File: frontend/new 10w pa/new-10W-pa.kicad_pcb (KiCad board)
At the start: 2 copper layers, 100 x 100 mm, 177 parts, among them K1 D3002, K2 D3002, K3 D3002, K4 D3002, K5 D3002, K6 D3002, P1 CONN_01X02, P2 CONN_02X01, P3 From HL CN3, P4 CONN_01X02, P5 CONN_01X02, P6 CONN_01X01, P7 From FE CN2, P8 CONN_01X08, P9 CONN_02X05, Q1 2N3906, Q3 RD16HHF1, T1 TRANSFO, T2 OUT_TRANSF, U1 74HC14, U2 74HC14, U3 TPIC6B595, U4 TPIC6B595, U5 TPIC6B595, U6 TPIC6B595, U7 LP2951-50D

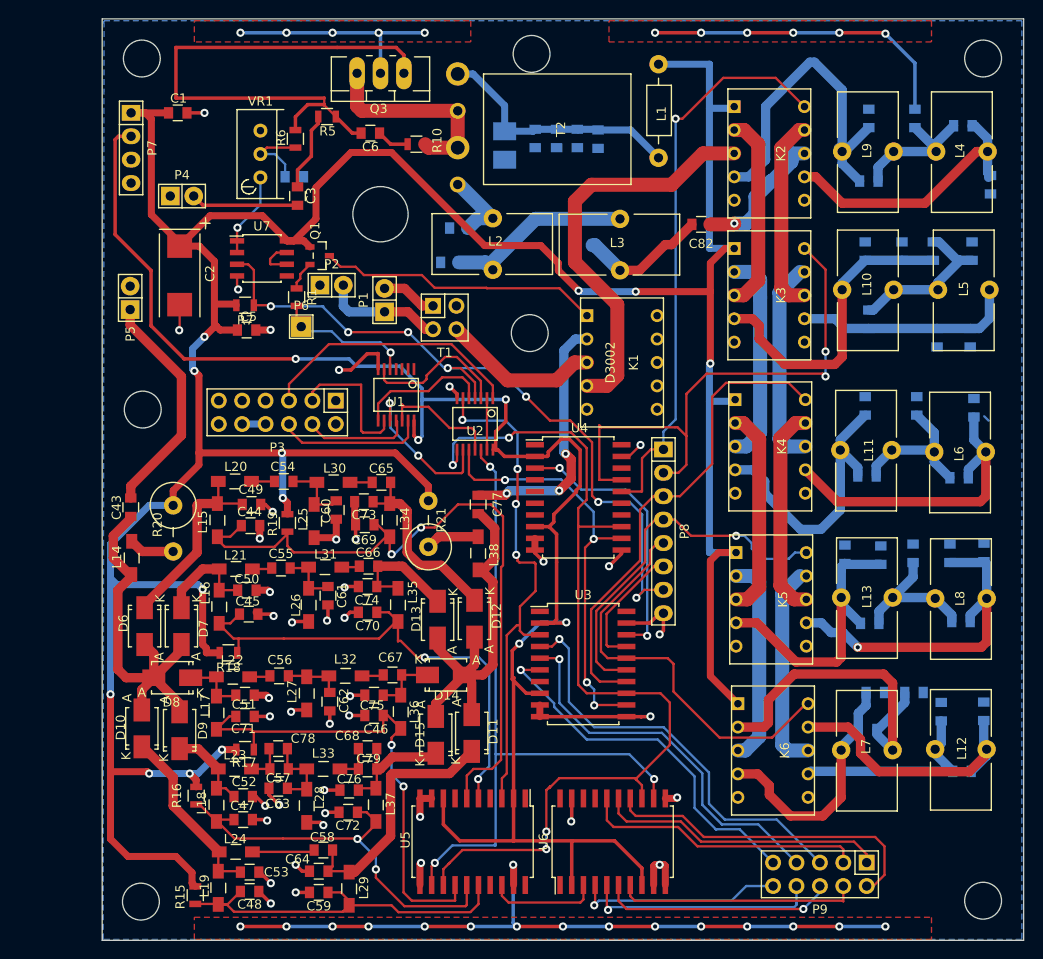
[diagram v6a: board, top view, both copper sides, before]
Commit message: Changes for new J16 approach
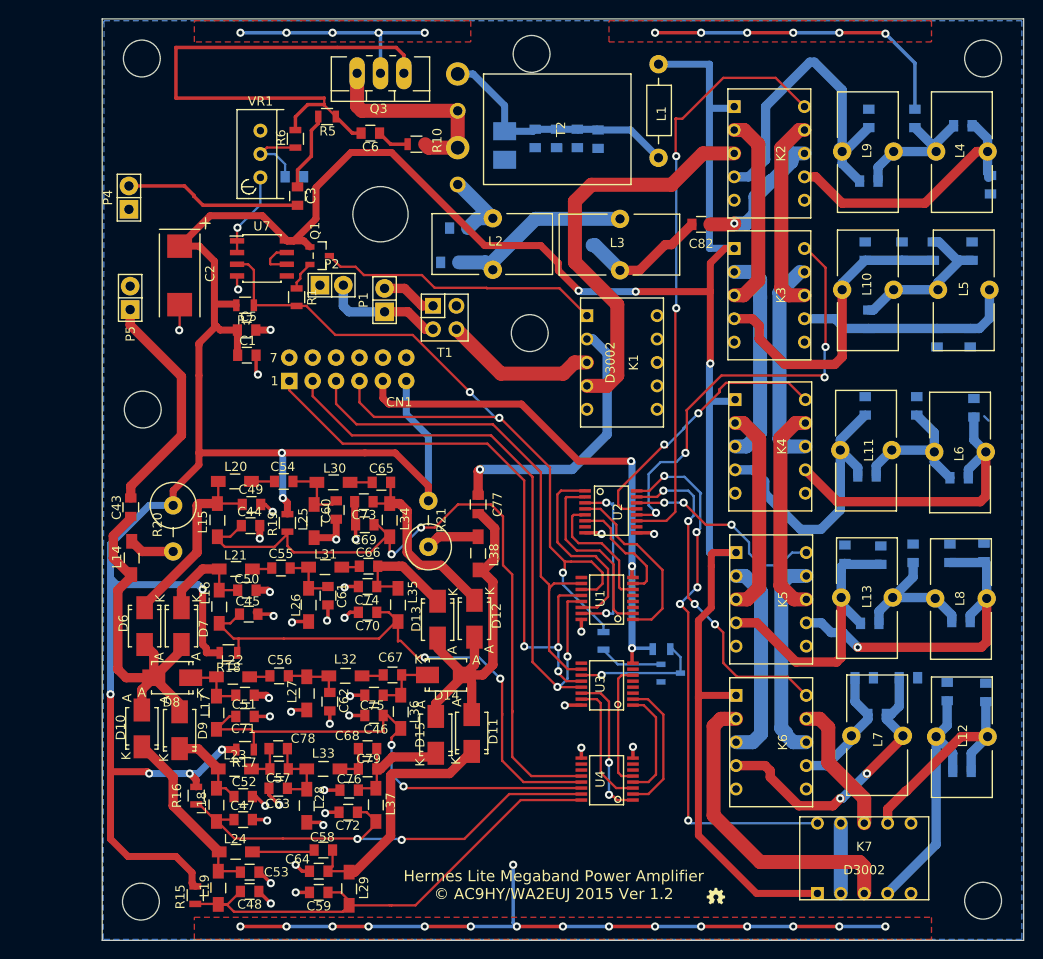
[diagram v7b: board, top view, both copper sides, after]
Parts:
- removed P3: From HL CN3, Pin_Headers:Pin_Header_Straight_2x06
- removed P6: CONN_01X01, Pin_Headers:Pin_Header_Straight_1x01
- removed P7: From FE CN2, Pin_Headers:Pin_Header_Straight_1x04
- removed P8: CONN_01X08, Pin_Headers:Pin_Header_Straight_1x08
- removed P9: CONN_02X05, Pin_Headers:Pin_Header_Straight_2x05
- removed U5, U6: TPIC6B595, Housings_SOIC:SOIC-20_7.5x12.8mm_Pitch1.27mm
- added CN1: BREAKOUT, HERMESLITE:BREAKOUT, F.Cu at (120.3, 89.3)
- added G***: OSHW-logo_silkscreen-front_2mm, HERMESLITE:OSHW-logo_silkscreen-front_2mm, F.Cu at (166.6, 145.2)
- added K7: D3002, HERMESLITE:D3002, F.Cu at (182.7, 141.1)
- added Q2: 2N3904, Transistors_SMD:sot23, B.Cu at (161.7, 121.0)
- added R2: 4.99k, HERMESLITE:R_0805, B.Cu at (154.4, 117.5)
- added R3: 4.99k, HERMESLITE:R_0805, B.Cu at (160.7, 118.4)
- U1: value 74HC14 -> 4028; footprint SMD_Packages:TSSOP-14 -> SMD_Packages:TSSOP-16
- U2: value 74HC14 -> ULN2003LV; footprint SMD_Packages:TSSOP-14 -> SMD_Packages:TSSOP-16
- U3: value TPIC6B595 -> 4028; footprint Housings_SOIC:SOIC-20_7.5x12.8mm_Pitch1.27mm -> SMD_Packages:TSSOP-16
- U4: value TPIC6B595 -> ULN2003LV; footprint Housings_SOIC:SOIC-20_7.5x12.8mm_Pitch1.27mm -> SMD_Packages:TSSOP-16
- moved U1 31.8 mm to (154.8, 112.9), turned to 90 degrees
- moved U4 30.7 mm to (154.8, 132.5), turned to 90 degrees
- moved C1 27.3 mm to (115.7, 86.5)
- moved U2 17.6 mm to (155.2, 103.5), turned to 270 degrees
- moved L7 15.8 mm to (180.8, 121.2), turned to 270 degrees
- moved P4 5.76 mm to (102.9, 69.4), turned to 90 degrees
- moved C20 5.63 mm to (182.7, 121.5)
- moved C26 3.94 mm to (187.5, 121.5)
- moved U3 3.40 mm to (154.8, 122.2), turned to 90 degrees
- moved C37 2.28 mm to (191.7, 123.0)
- moved C30 2.06 mm to (195.9, 123.1)
- moved C24 1.93 mm to (184.1, 125.5), turned to 180 degrees
- moved L12 1.37 mm to (196.6, 134.5)
- moved K6 0.92 mm to (172.6, 128.5)
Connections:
- K6 pad 2: Net-(C20-Pad1) -> Net-(K6-Pad2)
- K6 pad 7: Net-(C35-Pad1) -> Net-(C20-Pad1)
- K6 pad 9: Net-(C30-Pad1) -> Net-(K6-Pad9)
- R1 pad 2: Net-(P6-Pad1) -> #PTT
- R7 pad 1: /PTT -> #PTT
- U1 pad 10: Net-(U1-Pad10) -> A
- U1 pad 11: Net-(P3-Pad4) -> #PTT
- U1 pad 12: Net-(U1-Pad12) -> C
- U1 pad 13: Net-(P3-Pad6) -> B
- U1 pad 14: +5V -> Net-(U1-Pad14)
- U1 pad 5: Net-(P6-Pad1) -> Net-(U1-Pad5)
- U1 pad 7: GND -> Net-(U1-Pad7)
- U1 pad 8: Net-(U1-Pad8) -> 5V
- U2 pad 1: Net-(P3-Pad5) -> Net-(U1-Pad14)
- U2 pad 10: TX-Load -> Net-(U2-Pad10)
- U2 pad 11: Net-(U1-Pad12) -> Net-(K2-Pad10)
- U2 pad 12: RX-Load -> Net-(K3-Pad10)
- U2 pad 13: Net-(U2-Pad13) -> Net-(K4-Pad10)
- U2 pad 14: +5V -> Net-(K5-Pad10)
- U2 pad 2: Net-(U2-Pad13) -> Net-(U1-Pad2)
- U2 pad 3: Net-(U1-Pad6) -> Net-(U1-Pad15)
- U2 pad 4: /PTT -> Net-(U1-Pad1)
- U2 pad 5: Net-(U1-Pad8) -> Net-(U1-Pad6)
- U2 pad 6: SPI-DATA -> Net-(U1-Pad7)
- U2 pad 7: GND -> Net-(U2-Pad7)
- U2 pad 8: SPI-CLK -> GND
- U2 pad 9: Net-(U1-Pad10) -> GND
- U3 pad 1: (no net) -> Net-(U3-Pad1)
- U3 pad 10: GND -> A
- U3 pad 11: GND -> PTT
- U3 pad 12: TX-Load -> C
- U3 pad 13: SPI-CLK -> B
- U3 pad 14: Net-(K4-Pad10) -> Net-(U3-Pad14)
- U3 pad 15: Net-(K5-Pad10) -> Net-(U3-Pad15)
- U3 pad 16: Net-(K6-Pad10) -> GND
- U3 pad 2: +5V -> Net-(U3-Pad2)
- U3 pad 3: SPI-DATA -> Net-(U3-Pad3)
- U3 pad 4: ANT1 -> Net-(U3-Pad4)
- U3 pad 5: ANT2 -> Net-(U3-Pad5)
- U3 pad 6: ANT3 -> Net-(U3-Pad6)
- U3 pad 8: +5V -> 5V
- U3 pad 9: GND -> Net-(U3-Pad9)
- U4 pad 1: (no net) -> Net-(U3-Pad14)
- U4 pad 10: GND -> Net-(U4-Pad10)
- U4 pad 11: GND -> Net-(U4-Pad11)
- U4 pad 12: TX-Load -> Net-(C44-Pad1)
- U4 pad 13: SPI-CLK -> Net-(C45-Pad1)
- U4 pad 14: Net-(U4-Pad14) -> Net-(C46-Pad1)
- U4 pad 15: Net-(U4-Pad15) -> Net-(C47-Pad1)
- U4 pad 16: Net-(K2-Pad10) -> Net-(C48-Pad1)
- U4 pad 2: +5V -> Net-(U3-Pad2)
- U4 pad 3: Net-(U3-Pad18) -> Net-(U3-Pad15)
- U4 pad 4: Net-(U4-Pad4) -> Net-(U3-Pad1)
- U4 pad 5: Net-(U4-Pad5) -> Net-(U3-Pad6)
- U4 pad 8: +5V -> GND
- U7 pad 3: /PTT -> #PTT
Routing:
- net +5V: track 183.6 -> 0.00 mm, vias 5 -> 0
- net GND: track 251.3 -> 127.4 mm, vias 69 -> 47
- net SPI-CLK: track 105.4 -> 0.00 mm, vias 4 -> 0
- net #PTT: track 0.00 -> 92.5 mm, vias 0 -> 3
- net /PTT: track 79.0 -> 0.00 mm, vias 7 -> 0
- net (no net): track 0.67 -> 77.7 mm, vias 0 -> 16
- net RX-Load: track 74.1 -> 0.00 mm, vias 3 -> 0
- net B: track 0.00 -> 67.0 mm, vias 0 -> 2
- net C: track 0.00 -> 66.1 mm, vias 0 -> 3
- net Net-(K7-Pad10): track 0.00 -> 59.6 mm, vias 0 -> 5
- net 5V: track 0.00 -> 57.2 mm, vias 0 -> 3
- net A: track 0.00 -> 55.8 mm
- net SPI-DATA: track 55.7 -> 0.00 mm, vias 4 -> 0
- net TX-Load: track 46.4 -> 0.00 mm, vias 4 -> 0
- net ANT1: track 46.1 -> 0.00 mm, vias 1 -> 0
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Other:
- board text added: "Hermes Lite Megaband Power Amplifier © AC9HY/WA2EUJ 2015 Ver 1.2"
- board text removed: "AC9HY/WA2EUJ PA Ver 1.0"

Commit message: Final pcd changes
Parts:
- removed G***: OSHW-logo_silkscreen-front_2mm, HERMESLITE:OSHW-logo_silkscreen-front_2mm
- removed Q2: 2N3904, Transistors_SMD:sot23
- removed R1: 1k, HERMESLITE:R_0805
- removed R2, R3: 4.99k, HERMESLITE:R_0805
- removed R7: 10k, HERMESLITE:R_0805
- removed U4: ULN2003LV, SMD_Packages:TSSOP-16
- added C83: 1000pF, HERMESLITE:C_0805, F.Cu at (127.2, 94.6)
- added C84: 0.01uF, HERMESLITE:C_0805, F.Cu at (124.1, 95.5)
- added C85: 0.01uF, HERMESLITE:C_0805, F.Cu at (130.3, 95.8)
- added D1: DIODE, Diodes_SMD:Diode-SMA_Standard, F.Cu at (137.6, 142.0)
- added D16: DIODE, Diodes_SMD:Diode-SMA_Standard, F.Cu at (106.8, 114.4)
- added D17: DIODE, Diodes_SMD:Diode-SMA_Standard, F.Cu at (149.0, 113.7)
- added D2: DIODE, Diodes_SMD:Diode-SMA_Standard, F.Cu at (140.7, 137.2)
- added D3: DIODE, Diodes_SMD:Diode-SMA_Standard, F.Cu at (144.0, 135.2)
- added D4: DIODE, Diodes_SMD:Diode-SMA_Standard, F.Cu at (149.4, 126.0)
- added D5: DIODE, Diodes_SMD:Diode-SMA_Standard, F.Cu at (145.3, 94.4)
- added L39: 4700nH, HERMESLITE:Choke_SMD_1206_Standard, F.Cu at (119.9, 94.5)
- added L40: 4700uH, HERMESLITE:Choke_SMD_1206_Standard, F.Cu at (134.6, 94.6)
- added Q4: 2N7000, SMD_Packages:SOT-23-GDS, F.Cu at (140.1, 93.4)
- added R13: 1k, HERMESLITE:R_0805, F.Cu at (135.6, 91.6)
- added R14: 1k, HERMESLITE:R_0805, F.Cu at (119.9, 96.3)
- Q1: value 2N3906 -> 2N7000; footprint Transistors_SMD:sot23 -> SMD_Packages:SOT-23-GDS
- U1: value 4028 -> 4050; footprint SMD_Packages:TSSOP-16 -> Housings_SOIC:SOIC-16_3.9x9.9mm_Pitch1.27mm
- U2: value ULN2003LV -> 74LS145; footprint SMD_Packages:TSSOP-16 -> Housings_SOIC:SOIC-16_3.9x9.9mm_Pitch1.27mm
- U3: value 4028 -> 74LS145; footprint SMD_Packages:TSSOP-16 -> Housings_SOIC:SOIC-16_3.9x9.9mm_Pitch1.27mm
- moved CN1 65.0 mm to (161.3, 139.8), turned to 180 degrees
- moved U1 17.7 mm to (158.4, 130.2), turned to 0 degrees
- moved U3 9.94 mm to (158.3, 112.9), turned to 180 degrees
- moved R21 8.96 mm to (142.9, 99.9)
- moved L38 6.74 mm to (146.5, 104.4)
- moved C77 6.60 mm to (146.4, 99.2)
- moved C44 5.48 mm to (121.4, 103.6)
- moved C59 5.48 mm to (128.8, 143.4)
- moved C63 5.48 mm to (124.4, 132.1)
- moved C64 5.48 mm to (128.8, 141.1)
- moved C67 5.48 mm to (136.8, 119.8)
- moved C69 5.48 mm to (133.8, 103.5)
- moved C75 5.48 mm to (134.8, 122.0)
- moved D11 5.48 mm to (145.4, 126.1)
- moved D15 5.48 mm to (141.5, 126.3)
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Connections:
- CN1 pad 1: C -> Net-(CN1-Pad1)
- CN1 pad 2: B -> Net-(CN1-Pad2)
- CN1 pad 3: A -> Net-(CN1-Pad3)
- CN1 pad 4: #PTT -> Net-(CN1-Pad4)
- K1 pad 1: Net-(K1-Pad1) -> +12V
- K1 pad 10: GND -> Net-(K1-Pad10)
- U1 pad 1: Net-(U1-Pad1) -> 5V
- U1 pad 11: #PTT -> Net-(CN1-Pad4)
- U1 pad 12: C -> Net-(U1-Pad12)
- U1 pad 13: B -> (no net)
- U1 pad 14: Net-(U1-Pad14) -> (no net)
- U1 pad 15: Net-(U1-Pad15) -> (no net)
- U1 pad 16: GND -> (no net)
- U1 pad 2: Net-(U1-Pad2) -> D
- U1 pad 3: Net-(U1-Pad3) -> Net-(CN1-Pad7)
- U1 pad 4: Net-(U1-Pad4) -> C
- U1 pad 5: Net-(U1-Pad5) -> Net-(CN1-Pad1)
- U1 pad 6: Net-(U1-Pad6) -> B
- U1 pad 7: Net-(U1-Pad7) -> Net-(CN1-Pad2)
- U1 pad 8: 5V -> GND
- U1 pad 9: Net-(U1-Pad9) -> Net-(CN1-Pad3)
- U2 pad 1: Net-(U1-Pad14) -> Net-(K7-Pad10)
- U2 pad 10: Net-(U2-Pad10) -> Net-(K2-Pad10)
- U2 pad 12: Net-(K3-Pad10) -> D
- U2 pad 13: Net-(K4-Pad10) -> C
- U2 pad 14: Net-(K5-Pad10) -> B
- U2 pad 15: Net-(K6-Pad10) -> A
- U2 pad 16: Net-(K7-Pad10) -> 5V
- U2 pad 2: Net-(U1-Pad2) -> Net-(K6-Pad10)
- U2 pad 3: Net-(U1-Pad15) -> Net-(K5-Pad10)
- U2 pad 4: Net-(U1-Pad1) -> Net-(K5-Pad10)
- U2 pad 5: Net-(U1-Pad6) -> Net-(K4-Pad10)
- U2 pad 6: Net-(U1-Pad7) -> Net-(K4-Pad10)
- U2 pad 7: Net-(U2-Pad7) -> Net-(K3-Pad10)
- U2 pad 9: GND -> Net-(K3-Pad10)
- U3 pad 1: Net-(U3-Pad1) -> Net-(C48-Pad1)
- U3 pad 10: A -> Net-(C44-Pad1)
- U3 pad 11: PTT -> Net-(C44-Pad1)
- U3 pad 12: C -> D
- U3 pad 13: B -> C
- U3 pad 14: Net-(U3-Pad14) -> B
- U3 pad 15: Net-(U3-Pad15) -> A
- U3 pad 16: GND -> 5V
- U3 pad 2: Net-(U3-Pad2) -> Net-(C47-Pad1)
- U3 pad 3: Net-(U3-Pad3) -> Net-(C47-Pad1)
- U3 pad 4: Net-(U3-Pad4) -> Net-(C46-Pad1)
- U3 pad 5: Net-(U3-Pad5) -> Net-(C46-Pad1)
- U3 pad 6: Net-(U3-Pad6) -> Net-(C45-Pad1)
- U3 pad 7: Net-(U3-Pad7) -> Net-(C44-Pad1)
- U3 pad 8: 5V -> GND
- U3 pad 9: Net-(U3-Pad9) -> Net-(C44-Pad1)
- U7 pad 1: Net-(U7-Pad1) -> Net-(K1-Pad8)
- U7 pad 2: Net-(U7-Pad1) -> Net-(K1-Pad8)
- U7 pad 3: #PTT -> Net-(U1-Pad12)
- VR1 pad 1: Net-(U7-Pad1) -> Net-(K1-Pad7)
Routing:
- net Net-(U1-Pad12): track 0.00 -> 97.5 mm, vias 0 -> 4
- net #PTT: track 92.5 -> 0.00 mm, vias 3 -> 0
- net Net-(D1-Pad1): track 0.00 -> 75.0 mm
- net Net-(K1-Pad7): track 0.00 -> 72.9 mm, vias 0 -> 3
- net Net-(K1-Pad8): track 0.00 -> 63.4 mm
- net +12V: track 379.7 -> 437.4 mm
- net D: track 0.00 -> 47.3 mm, vias 0 -> 3
- net Net-(K1-Pad10): track 0.00 -> 40.1 mm, vias 0 -> 1
- net Net-(CN1-Pad7): track 0.00 -> 36.8 mm, vias 0 -> 2
- net Net-(C83-Pad2): track 0.00 -> 35.7 mm
- net Net-(C83-Pad1): track 0.00 -> 34.1 mm
- net Net-(K1-Pad1): track 30.6 -> 0.00 mm
- net C: track 66.1 -> 41.3 mm
- net Net-(C84-Pad1): track 0.00 -> 23.8 mm, vias 0 -> 2
- net Net-(U1-Pad14): track 21.6 -> 0.00 mm
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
